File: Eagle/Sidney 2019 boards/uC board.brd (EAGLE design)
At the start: 100 x 100 mm, 55 parts, among them J1 39-28-1043

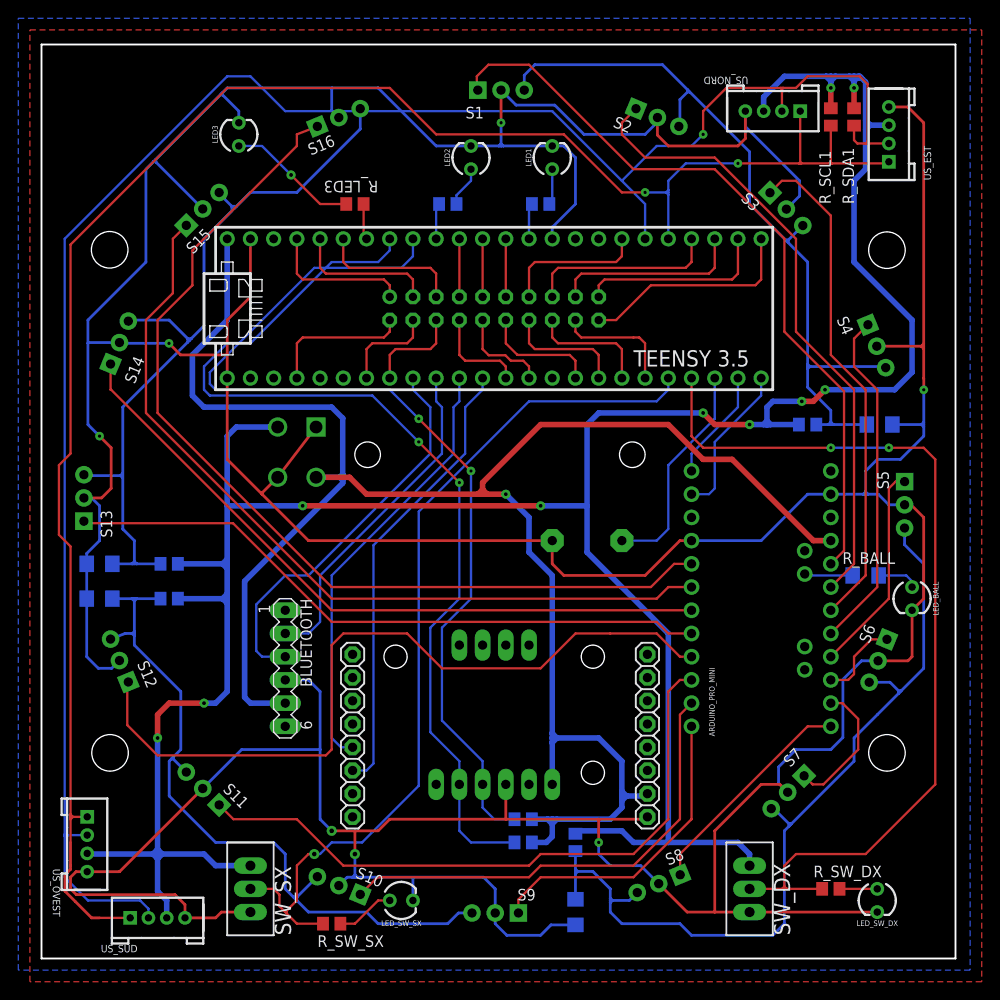
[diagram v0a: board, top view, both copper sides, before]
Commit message: Finished components lists for both boards and fixed line sensors' connectors pinout
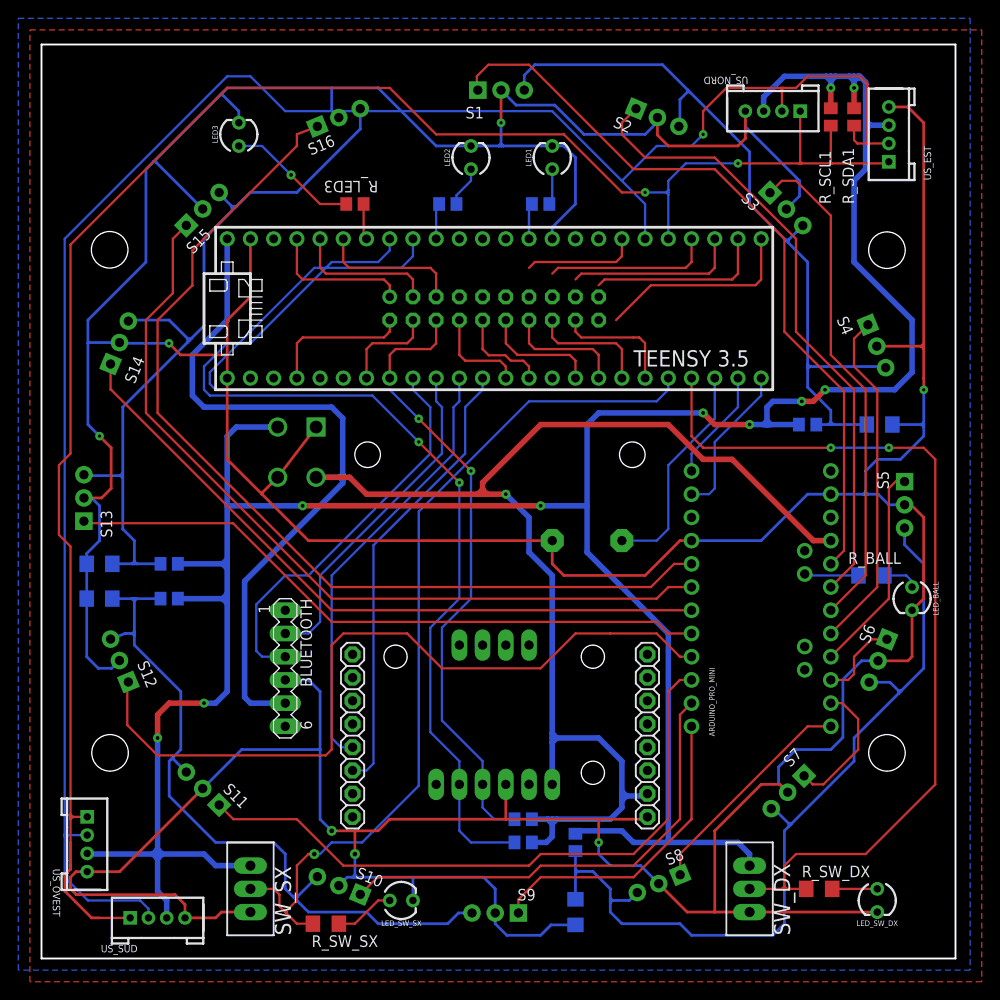
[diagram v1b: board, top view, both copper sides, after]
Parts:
- R_SW_DX, R_SW_SX: device rcl:R0805 -> rcl:R1206
- moved R_SW_DX 1.27 mm to (85.1, 7.62)
- moved R_BALL 0.64 mm to (90.8, 41.9)
- moved R_SW_SX 0.64 mm to (31.1, 3.81)
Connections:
- new net S1_IN: SIGN_CON.20
- new net S1_OUT: SIGN_CON.19
- new net S2_IN: SIGN_CON.17
- new net S2_OUT: SIGN_CON.15
- new net S3_IN: SIGN_CON.13
- new net S3_OUT: SIGN_CON.11
- new net S4_IN: SIGN_CON.9
- new net S4_OUT: SIGN_CON.7
- net S1_DOWN: no longer SIGN_CON.19
- net S1_UP: no longer SIGN_CON.20
- net S2_DOWN: no longer SIGN_CON.15
- net S2_UP: no longer SIGN_CON.17
- net S3_DOWN: no longer SIGN_CON.11
- net S3_UP: no longer SIGN_CON.13
- net S4_DOWN: no longer SIGN_CON.7
- net S4_UP: no longer SIGN_CON.9
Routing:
- net S4_UP: track 6.35 -> 0.00 mm
- net S4_DOWN: track 6.35 -> 0.00 mm
- net S3_DOWN: track 6.35 -> 0.00 mm
- net S3_UP: track 15.8 -> 12.6 mm
- net S2_DOWN: track 20.8 -> 18.3 mm
- net S2_UP: track 20.8 -> 18.9 mm
- net S1_UP: track 24.1 -> 22.2 mm
- net SW_DX: track 100.8 -> 99.0 mm
- net S1_DOWN: track 20.8 -> 19.6 mm
- net SW_SX: track 97.4 -> 96.3 mm
- net N$11: track 4.13 -> 4.93 mm
- net N$3: track 4.56 -> 3.92 mm
- net N$4: track 5.31 -> 5.95 mm
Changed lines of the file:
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@@
 <attribute name="NAME" x="27.305" y="2.54" size="1.778" layer="25" rot="R90"/>
 </element>
-<element name="R_SW_SX" library="rcl" library_urn="urn:adsk.eagle:library:334" package="R0805" package3d_urn="urn:adsk.eagle:package:23553/2" value="330" x="31.75" y="3.81" smashed="yes" rot="R180">
-<attribute name="NAME" x="37.465" y="2.54" size="1.27" layer="25" rot="R180"/>
-<attribute name="SPICEPREFIX" value="R" x="31.75" y="3.81" size="1.778" layer="27" rot="R180" display="off"/>
+<element name="R_SW_SX" library="rcl" library_urn="urn:adsk.eagle:library:334" package="R1206" package3d_urn="urn:adsk.eagle:package:23540/2" value="330" x="31.115" y="3.81" smashed="yes" rot="R180">
+<attribute name="NAME" x="36.83" y="2.54" size="1.27" layer="25" rot="R180"/>
+<attribute name="SPICEPREFIX" value="R" x="31.115" y="3.81" size="1.778" layer="27" rot="R180" display="off"/>
 </element>
 <element name="LED_SW_SX" library="SparkFun-LED" package="LED_3MM" value="" x="39.37" y="6.35" smashed="yes">
@@
 <attribute name="VALUE" x="72.39" y="12.7" size="1.778" layer="27" rot="R270"/>
 </element>
-<element name="R_SW_DX" library="rcl" library_urn="urn:adsk.eagle:library:334" package="R0805" package3d_urn="urn:adsk.eagle:package:23553/2" value="330" x="86.36" y="7.62" smashed="yes" rot="R180">
-<attribute name="NAME" x="84.455" y="8.89" size="1.27" layer="25"/>
-<attribute name="SPICEPREFIX" value="R" x="97.79" y="-3.81" size="1.778" layer="27" rot="R180" display="off"/>
+<element name="R_SW_DX" library="rcl" library_urn="urn:adsk.eagle:library:334" package="R1206" package3d_urn="urn:adsk.eagle:package:23540/2" value="330" x="85.09" y="7.62" smashed="yes" rot="R180">
+<attribute name="NAME" x="83.185" y="8.89" size="1.27" layer="25"/>
+<attribute name="SPICEPREFIX" value="R" x="96.52" y="-3.81" size="1.778" layer="27" rot="R180" display="off"/>
 </element>
 <element name="LED_SW_DX" library="SparkFun-LED" package="LED_3MM" value="" x="91.44" y="6.35" smashed="yes" rot="R270">
@@
 <attribute name="SPICEPREFIX" value="R" x="88.9" y="92.075" size="1.778" layer="27" rot="R90" display="off"/>
 </element>
-<element name="R_BALL" library="rcl" library_urn="urn:adsk.eagle:library:334" package="R1206" package3d_urn="urn:adsk.eagle:package:23540/2" value="330" x="90.17" y="41.91" smashed="yes" rot="MR0">
-<attribute name="NAME" x="87.63" y="43.18" size="1.27" layer="25"/>
-<attribute name="SPICEPREFIX" value="R" x="90.17" y="41.91" size="1.778" layer="28" rot="MR0" display="off"/>
-<attribute name="VALUE" x="88.9" y="39.37" size="1.27" layer="27"/>
+<element name="R_BALL" library="rcl" library_urn="urn:adsk.eagle:library:334" package="R1206" package3d_urn="urn:adsk.eagle:package:23540/2" value="330" x="90.805" y="41.91" smashed="yes" rot="MR0">
+<attribute name="NAME" x="88.265" y="43.18" size="1.27" layer="25"/>
+<attribute name="SPICEPREFIX" value="R" x="90.805" y="41.91" size="1.778" layer="28" rot="MR0" display="off"/>
+<attribute name="VALUE" x="89.535" y="39.37" size="1.27" layer="27"/>
 </element>
 <element name="J1" library="39-28-1043" package="39-28-1043" value="39-28-1043" x="27.94" y="50.8" smashed="yes" rot="MR0">
@@
 <signal name="S1_UP">
 <contactref element="TEENSY_3.5" pad="33/A14"/>
-<contactref element="SIGN_CON" pad="20"/>
 <wire x1="62.865" y1="69.85" x2="66.675" y2="73.66" width="0.254" layer="1"/>
-<wire x1="60.96" y1="69.85" x2="62.865" y2="69.85" width="0.254" layer="1"/>
 <wire x1="78.74" y1="78.74" x2="78.74" y2="74.295" width="0.254" layer="1"/>
 <wire x1="78.105" y1="73.66" x2="78.74" y2="74.295" width="0.254" layer="1"/>
@@
 <signal name="S1_DOWN">
 <contactref element="TEENSY_3.5" pad="34/A15"/>
-<contactref element="SIGN_CON" pad="19"/>
-<wire x1="60.96" y1="72.39" x2="60.96" y2="73.66" width="0.254" layer="1"/>
 <wire x1="60.96" y1="73.66" x2="61.595" y2="74.295" width="0.254" layer="1"/>
 <wire x1="76.2" y1="78.74" x2="76.2" y2="74.93" width="0.254" layer="1"/>
@@
 <signal name="S2_UP">
 <contactref element="TEENSY_3.5" pad="35/A16"/>
-<contactref element="SIGN_CON" pad="17"/>
 <wire x1="59.055" y1="74.93" x2="58.42" y2="74.295" width="0.254" layer="1"/>
 <wire x1="73.66" y1="75.565" x2="73.025" y2="74.93" width="0.254" layer="1"/>
 <wire x1="59.055" y1="74.93" x2="73.025" y2="74.93" width="0.254" layer="1"/>
-<wire x1="58.42" y1="74.295" x2="58.42" y2="72.39" width="0.254" layer="1"/>
 <wire x1="73.66" y1="78.74" x2="73.66" y2="75.565" width="0.254" layer="1"/>
 </signal>
 <signal name="S2_DOWN">
 <contactref element="TEENSY_3.5" pad="36/A17"/>
-<contactref element="SIGN_CON" pad="15"/>
-<wire x1="55.88" y1="72.39" x2="55.88" y2="74.93" width="0.254" layer="1"/>
 <wire x1="55.88" y1="74.93" x2="56.515" y2="75.565" width="0.254" layer="1"/>
 <wire x1="56.515" y1="75.565" x2="70.485" y2="75.565" width="0.254" layer="1"/>
@@
 <signal name="S4_DOWN">
 <contactref element="TEENSY_3.5" pad="16/A2"/>
-<contactref element="SIGN_CON" pad="7"/>
-<wire x1="45.72" y1="72.39" x2="45.72" y2="78.74" width="0.254" layer="1"/>
 </signal>
 <signal name="S4_UP">
 <contactref element="TEENSY_3.5" pad="15/A1"/>
-<contactref element="SIGN_CON" pad="9"/>
-<wire x1="48.26" y1="72.39" x2="48.26" y2="78.74" width="0.254" layer="1"/>
 </signal>
 <signal name="S3_UP">
 <contactref element="TEENSY_3.5" pad="39/A20"/>
-<contactref element="SIGN_CON" pad="13"/>
 <wire x1="63.5" y1="78.74" x2="63.5" y2="76.835" width="0.254" layer="1"/>
 <wire x1="62.865" y1="76.2" x2="63.5" y2="76.835" width="0.254" layer="1"/>
-<wire x1="53.34" y1="72.39" x2="53.34" y2="75.565" width="0.254" layer="1"/>
 <wire x1="53.34" y1="75.565" x2="53.975" y2="76.2" width="0.254" layer="1"/>
 <wire x1="53.975" y1="76.2" x2="62.865" y2="76.2" width="0.254" layer="1"/>
@@
 <signal name="S3_DOWN">
 <contactref element="TEENSY_3.5" pad="14/A0"/>
-<contactref element="SIGN_CON" pad="11"/>
-<wire x1="50.8" y1="72.39" x2="50.8" y2="78.74" width="0.254" layer="1"/>
 </signal>
 <signal name="SDA_I2C">
@@
 <wire x1="26.67" y1="5.08" x2="26.797" y2="4.953" width="0.254" layer="1"/>
 <wire x1="26.797" y1="4.953" x2="27.94" y2="3.81" width="0.254" layer="1"/>
-<wire x1="27.94" y1="3.81" x2="30.8" y2="3.81" width="0.254" layer="1"/>
+<wire x1="27.94" y1="3.81" x2="29.693" y2="3.81" width="0.254" layer="1"/>
 <wire x1="68.58" y1="63.5" x2="68.58" y2="62.23" width="0.254" layer="16"/>
 <wire x1="68.58" y1="62.23" x2="67.31" y2="60.96" width="0.254" layer="16"/>
@@
 <wire x1="77.47" y1="7.62" x2="81.026" y2="7.62" width="0.254" layer="1"/>
 <wire x1="81.026" y1="7.62" x2="81.534" y2="7.62" width="0.254" layer="1"/>
-<wire x1="81.534" y1="7.62" x2="85.41" y2="7.62" width="0.254" layer="1"/>
+<wire x1="81.534" y1="7.62" x2="83.668" y2="7.62" width="0.254" layer="1"/>
 <wire x1="81.026" y1="7.62" x2="81.28" y2="7.874" width="0.254" layer="1"/>
 <wire x1="81.28" y1="7.874" x2="81.534" y2="7.62" width="0.254" layer="1"/>
@@
 <contactref element="LED_BALL" pad="A"/>
 <contactref element="R_BALL" pad="1"/>
-<wire x1="91.592" y1="41.91" x2="94.615" y2="41.91" width="0.254" layer="16"/>
+<wire x1="92.227" y1="41.91" x2="94.615" y2="41.91" width="0.254" layer="16"/>
 <wire x1="94.615" y1="41.91" x2="95.25" y2="41.275" width="0.254" layer="16"/>
 <wire x1="95.25" y1="41.275" x2="95.25" y2="40.64" width="0.254" layer="16"/>
@@
 <contactref element="ARDUINO_PRO_MINI" pad="A4"/>
 <contactref element="R_BALL" pad="2"/>
-<wire x1="88.748" y1="41.91" x2="83.66125" y2="41.91" width="0.254" layer="16"/>
+<wire x1="89.383" y1="41.91" x2="83.66125" y2="41.91" width="0.254" layer="16"/>
 <wire x1="83.66125" y1="41.91" x2="83.5025" y2="42.06875" width="0.254" layer="16"/>
 </signal>
@@
 <contactref element="LED_SW_SX" pad="A"/>
 <wire x1="36.83" y1="6.35" x2="38.1" y2="6.35" width="0.254" layer="1"/>
-<wire x1="32.7" y1="3.81" x2="34.29" y2="3.81" width="0.254" layer="1"/>
+<wire x1="32.537" y1="3.81" x2="34.29" y2="3.81" width="0.254" layer="1"/>
 <wire x1="34.29" y1="3.81" x2="36.83" y2="6.35" width="0.254" layer="1"/>
 </signal>
@@
 <contactref element="R_SW_DX" pad="1"/>
 <contactref element="LED_SW_DX" pad="A"/>
-<wire x1="87.31" y1="7.62" x2="91.44" y2="7.62" width="0.254" layer="1"/>
+<wire x1="86.512" y1="7.62" x2="91.44" y2="7.62" width="0.254" layer="1"/>
 </signal>
 <signal name="SDA1">
@@
 <wire x1="58.74" y1="13.97" x2="58.42" y2="13.65" width="0.6096" layer="16"/>
 </signal>
+<signal name="S1_IN">
+<contactref element="SIGN_CON" pad="20"/>
+</signal>
+<signal name="S1_OUT">
+<contactref element="SIGN_CON" pad="19"/>
+</signal>
+<signal name="S2_IN">
+<contactref element="SIGN_CON" pad="17"/>
+</signal>
+<signal name="S2_OUT">
+<contactref element="SIGN_CON" pad="15"/>
+</signal>
+<signal name="S3_IN">
+<contactref element="SIGN_CON" pad="13"/>
+</signal>
+<signal name="S3_OUT">
+<contactref element="SIGN_CON" pad="11"/>
+</signal>
+<signal name="S4_IN">
+<contactref element="SIGN_CON" pad="9"/>
+</signal>
+<signal name="S4_OUT">
+<contactref element="SIGN_CON" pad="7"/>
+</signal>
 </signals>
